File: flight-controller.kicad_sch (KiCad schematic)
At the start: 21 parts, among them U1 STM32WB55CEUx, X1 32MHz, X2 32kHz768

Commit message: added gitignore, schematic updated
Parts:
- added C16, C17: 100n, symbol Device:C
- added C18, C19: 4.7uF, symbol Device:C
- added J1: Conn_Coaxial, symbol Connector:Conn_Coaxial
- added J2: TC2030, Connector:Tag-Connect_TC2030-IDC-FP_2x03_P1.27mm_Vertical, symbol Connector:Conn_ARM_SWD_TagConnect_TC2030
- added J3: USB_C_Receptacle_USB2.0_16P, symbol Connector:USB_C_Receptacle_USB2.0_16P
- added R1, R3, R4: 5k1, symbol Device:R
- added R2: 100, symbol Device:R
- added SW1: SW_Push, symbol Switch:SW_Push
- added U2: DLF162500LT-5028A1, DLF-4_1P6X0P8, symbol TDK_LPF:DLF162500LT-5028A1
- added U3: USBLC6-2SC6, Package_TO_SOT_SMD:SOT-23-6, symbol Power_Protection:USBLC6-2SC6
- added U4: MIC5365-3.3YD5, Package_TO_SOT_SMD:SOT-23-5, symbol Regulator_Linear:MIC5365-3.3YD5
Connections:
- net +3V3: now also C19.1, J2.1 (VCC), SW1.2, U4.5 (VOUT)
- net GND: now also C16.2, C17.2, C18.2, C19.2, J1.2 (Ext), J2.5 (GND), J3.A1 (GND), J3.A12 (GND), J3.B1 (GND), J3.B12 (GND), J3.S1 (SHIELD), R1.2, R3.2, R4.2, U2.2 (GND), U2.4 (GND), U3.2 (GND), U4.2 (GND)
- net RF_MATCH: now reaches C15.1, L3.2
- net RF_MATCH: now also U2.1 (IN)
- net USB_D-: now reaches U1.37 (PA11)
- net USB_D-: now also U3.6 (I/O1)
- net USB_D+: now reaches U1.38 (PA12)
- net USB_D+: now also U3.4 (I/O2)
- net SWD_DIO: now reaches U1.39 (PA13)
- net SWD_DIO: now also J2.2 (SWDIO)
- net BOOT0: now reaches U1.4 (PH3)
- net BOOT0: now also C17.1, R1.1, R2.1
- net SWCLK: now reaches U1.41 (PA14)
- net SWCLK: now also J2.4 (SWCLK)
- net at U1.43 (PB3): now also J2.6 (SWO)
- net SWD_NRST: now reaches U1.7 (NRST)
- net SWD_NRST: now also C16.1, J2.3 (~{RESET})
- new net: R2.2, SW1.1
- new net: J3.B5 (CC2), R3.1
- new net: J3.A5 (CC1), R4.1
- new net: J3.A7 (D-), J3.B7 (D-), U3.1 (I/O1)
- new net: J3.A6 (D+), J3.B6 (D+), U3.3 (I/O2)
- new net +5V: C18.1, J3.A4 (VBUS), J3.A9 (VBUS), J3.B4 (VBUS), J3.B9 (VBUS), U3.5 (VBUS), U4.1 (VIN), U4.3 (EN)
- new net RF_NET: J1.1 (In), U2.3 (OUT)
- no-connect marks 0 -> 2
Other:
- moved on the sheet: C1, C10, C11, C12, C13, C14, C15, C2, C3, C4, C5, C6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

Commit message: added outline of imu, wip
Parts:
- added C20: 10n, symbol Device:C
- added C21, C22: 100n, symbol Device:C
- added C23: 2n2, symbol Device:C
- added R5, R6: 2k2, symbol Device:R
- added U5: MPU-6050, Sensor_Motion:InvenSense_QFN-24_4x4mm_P0.5mm, symbol Sensor_Motion:MPU-6050
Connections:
- net +3V3: now also C20.1, C21.1, R5.2, R6.2, U5.13 (VDD), U5.8 (VLOGIC)
- net GND: now also C20.2, C21.2, C22.2, C23.2, U5.1 (CLKIN), U5.11 (FSYNC), U5.18 (GND), U5.9 (AD0)
- net SCL: now reaches U1.5 (PB8)
- net SCL: now also R5.1, U5.23 (SCL)
- net SDA: now reaches U1.6 (PB9)
- net SDA: now also R6.1, U5.24 (SDA)
- new net: C22.1, U5.10 (REGOUT)
- new net: C23.1, U5.20 (CPOUT)
- no-connect marks 2 -> 4

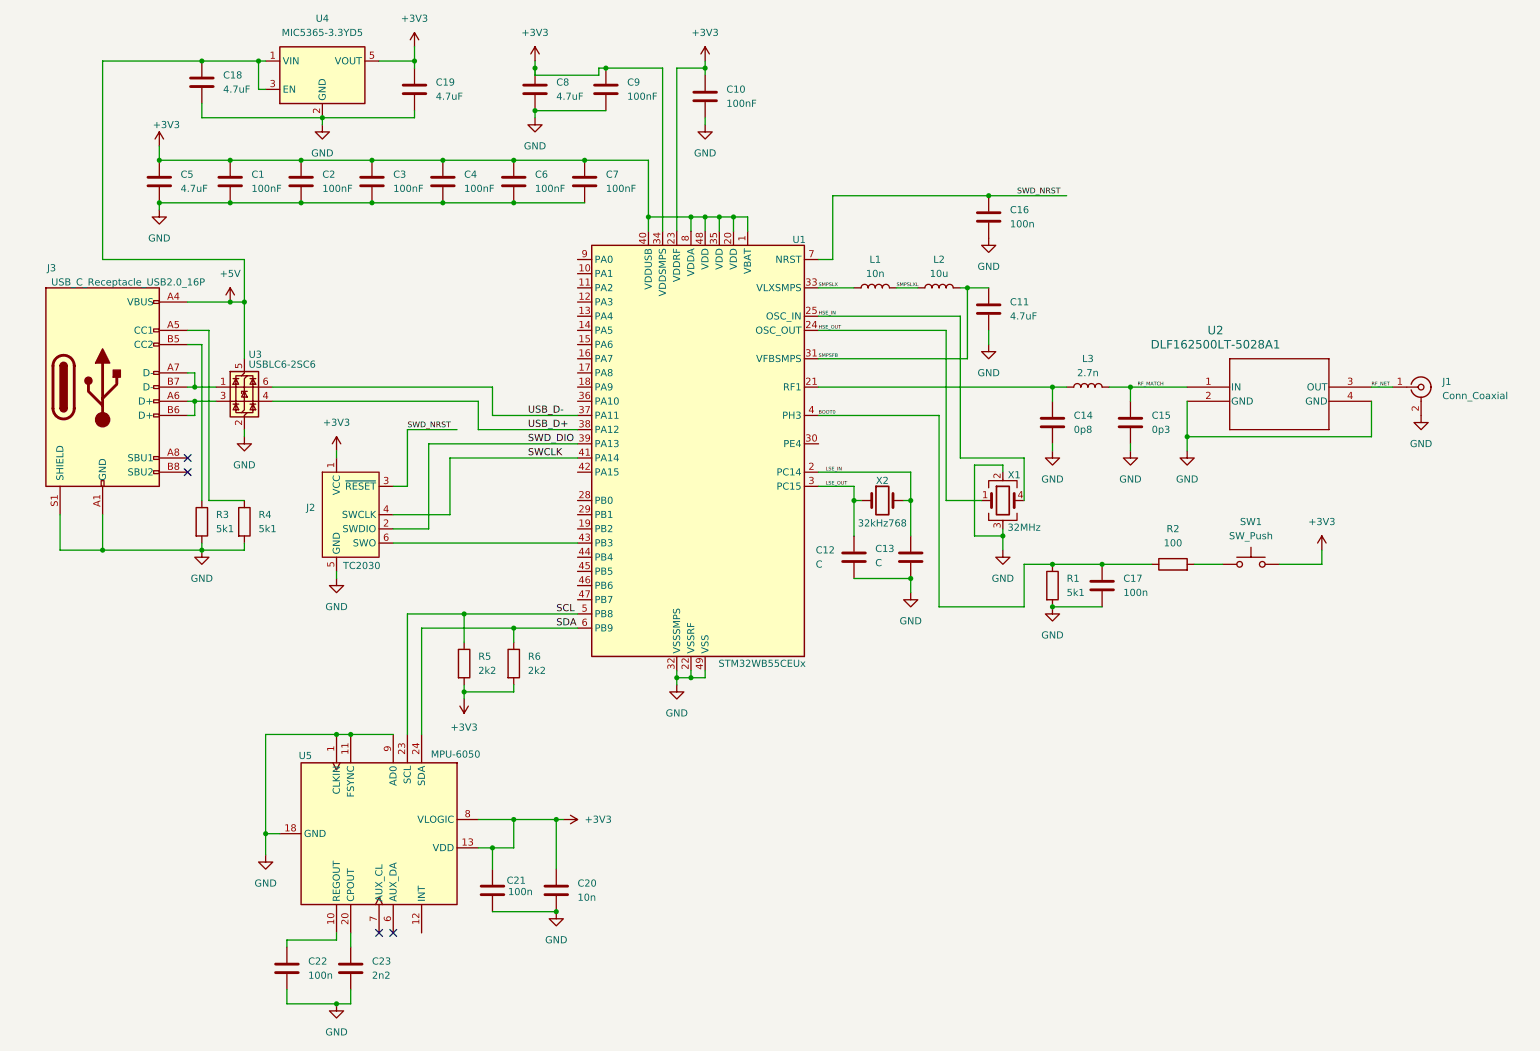
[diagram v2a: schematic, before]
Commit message: added footprints, started BOM
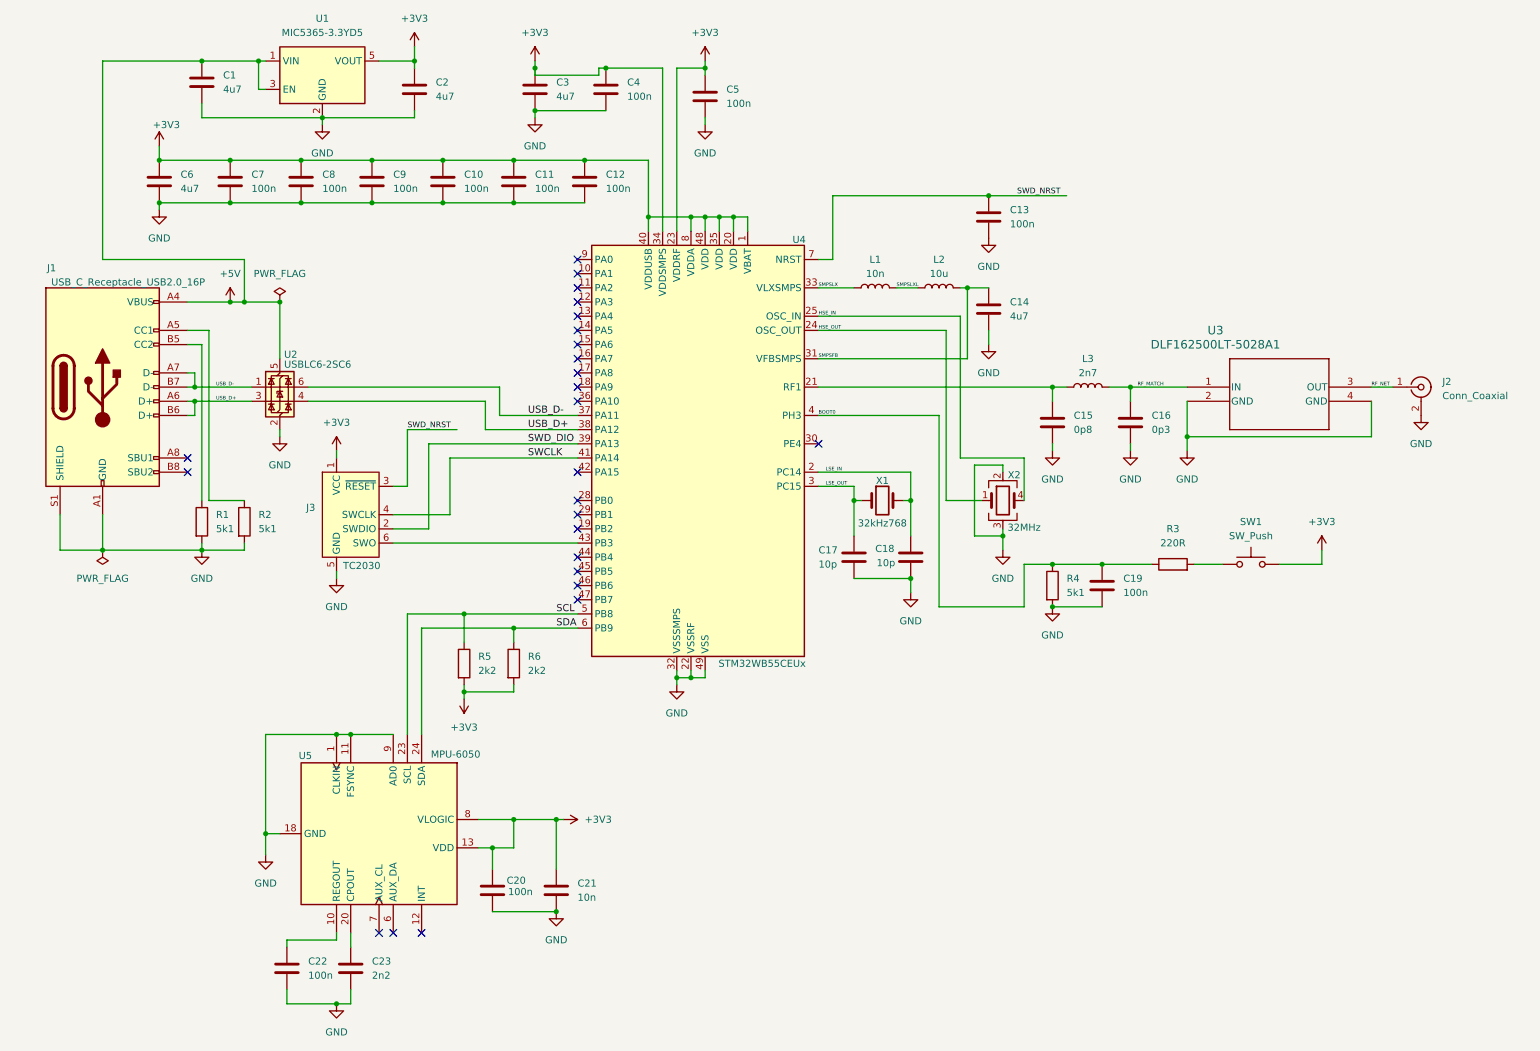
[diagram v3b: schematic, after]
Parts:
- C1: renamed from C18; value 4.7uF -> 4u7; footprint (none) -> Capacitor_SMD:C_0603_1608Metric; Distributor Link (none) -> https://www.mouser.com/ProductDetail/KYOCERA-AVX/0603ZD475M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; Manufacturer (none) -> Kyocera AVX; Manufacturer Part # (none) -> 0603ZD475MAT2A
- C10: renamed from C4; value 100nF -> 100n; footprint (none) -> Capacitor_SMD:C_0402_1005Metric; Distributor Link (none) -> https://www.mouser.com/ProductDetail/KYOCERA-AVX/0402X7R104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; Manufacturer (none) -> Kyocera AVX; Manufacturer Part # (none) -> 0402X7R104KT7AT
- C11: renamed from C6; value 100nF -> 100n; footprint (none) -> Capacitor_SMD:C_0402_1005Metric; Distributor Link (none) -> https://www.mouser.com/ProductDetail/KYOCERA-AVX/0402X7R104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; Manufacturer (none) -> Kyocera AVX; Manufacturer Part # (none) -> 0402X7R104KT7AT
- C12: renamed from C7; value 100nF -> 100n; footprint (none) -> Capacitor_SMD:C_0402_1005Metric; Distributor Link (none) -> https://www.mouser.com/ProductDetail/KYOCERA-AVX/0402X7R104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; Manufacturer (none) -> Kyocera AVX; Manufacturer Part # (none) -> 0402X7R104KT7AT
- C13: renamed from C16; footprint (none) -> Capacitor_SMD:C_0402_1005Metric; Distributor Link (none) -> https://www.mouser.com/ProductDetail/KYOCERA-AVX/0402X7R104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; Manufacturer (none) -> Kyocera AVX; Manufacturer Part # (none) -> 0402X7R104KT7AT
- C14: renamed from C11; value 4.7uF -> 4u7; footprint (none) -> Capacitor_SMD:C_0603_1608Metric; Distributor Link (none) -> https://www.mouser.com/ProductDetail/KYOCERA-AVX/0603ZD475M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; Manufacturer (none) -> Kyocera AVX; Manufacturer Part # (none) -> 0603ZD475MAT2A
- C15: renamed from C14; footprint (none) -> Capacitor_SMD:C_0402_1005Metric
- C16: renamed from C15; footprint (none) -> Capacitor_SMD:C_0402_1005Metric
- C17: renamed from C12; value C -> 10p; footprint (none) -> Capacitor_SMD:C_0402_1005Metric
- C18: renamed from C13; value C -> 10p; footprint (none) -> Capacitor_SMD:C_0402_1005Metric
- C19: renamed from C17; footprint (none) -> Capacitor_SMD:C_0402_1005Metric; Distributor Link (none) -> https://www.mouser.com/ProductDetail/KYOCERA-AVX/0402X7R104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; Manufacturer (none) -> Kyocera AVX; Manufacturer Part # (none) -> 0402X7R104KT7AT
- C2: renamed from C19; value 4.7uF -> 4u7; footprint (none) -> Capacitor_SMD:C_0603_1608Metric; Distributor Link (none) -> https://www.mouser.com/ProductDetail/KYOCERA-AVX/0603ZD475M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; Manufacturer (none) -> Kyocera AVX; Manufacturer Part # (none) -> 0603ZD475MAT2A
- C20: renamed from C21; footprint (none) -> Capacitor_SMD:C_0402_1005Metric; Distributor Link (none) -> https://www.mouser.com/ProductDetail/KYOCERA-AVX/0402X7R104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; Manufacturer (none) -> Kyocera AVX; Manufacturer Part # (none) -> 0402X7R104KT7AT
- C21: renamed from C20; footprint (none) -> Capacitor_SMD:C_0402_1005Metric
- C22: footprint (none) -> Capacitor_SMD:C_0402_1005Metric; Distributor Link (none) -> https://www.mouser.com/ProductDetail/KYOCERA-AVX/0402X7R104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; Manufacturer (none) -> Kyocera AVX; Manufacturer Part # (none) -> 0402X7R104KT7AT
- C23: footprint (none) -> Capacitor_SMD:C_0402_1005Metric
- C3: renamed from C8; value 4.7uF -> 4u7; footprint (none) -> Capacitor_SMD:C_0603_1608Metric; Distributor Link (none) -> https://www.mouser.com/ProductDetail/KYOCERA-AVX/0603ZD475M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; Manufacturer (none) -> Kyocera AVX; Manufacturer Part # (none) -> 0603ZD475MAT2A
- C4: renamed from C9; value 100nF -> 100n; footprint (none) -> Capacitor_SMD:C_0402_1005Metric; Distributor Link (none) -> https://www.mouser.com/ProductDetail/KYOCERA-AVX/0402X7R104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; Manufacturer (none) -> Kyocera AVX; Manufacturer Part # (none) -> 0402X7R104KT7AT
- C5: renamed from C10; value 100nF -> 100n; footprint (none) -> Capacitor_SMD:C_0402_1005Metric; Distributor Link (none) -> https://www.mouser.com/ProductDetail/KYOCERA-AVX/0402X7R104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; Manufacturer (none) -> Kyocera AVX; Manufacturer Part # (none) -> 0402X7R104KT7AT
- C6: renamed from C5; value 4.7uF -> 4u7; footprint (none) -> Capacitor_SMD:C_0603_1608Metric; Distributor Link (none) -> https://www.mouser.com/ProductDetail/KYOCERA-AVX/0603ZD475M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; Manufacturer (none) -> Kyocera AVX; Manufacturer Part # (none) -> 0603ZD475MAT2A
- C7: renamed from C1; value 100nF -> 100n; footprint (none) -> Capacitor_SMD:C_0402_1005Metric; Distributor Link (none) -> https://www.mouser.com/ProductDetail/KYOCERA-AVX/0402X7R104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; Manufacturer (none) -> Kyocera AVX; Manufacturer Part # (none) -> 0402X7R104KT7AT
- C8: renamed from C2; value 100nF -> 100n; footprint (none) -> Capacitor_SMD:C_0402_1005Metric; Distributor Link (none) -> https://www.mouser.com/ProductDetail/KYOCERA-AVX/0402X7R104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; Manufacturer (none) -> Kyocera AVX; Manufacturer Part # (none) -> 0402X7R104KT7AT
- C9: renamed from C3; value 100nF -> 100n; footprint (none) -> Capacitor_SMD:C_0402_1005Metric; Distributor Link (none) -> https://www.mouser.com/ProductDetail/KYOCERA-AVX/0402X7R104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; Manufacturer (none) -> Kyocera AVX; Manufacturer Part # (none) -> 0402X7R104KT7AT
- J1: renamed from J3; footprint (none) -> Connector_USB:USB_C_Receptacle_GCT_USB4105-xx-A_16P_TopMnt_Horizontal
- J2: renamed from J1; footprint (none) -> Connector_Coaxial:U.FL_Hirose_U.FL-R-SMT-1_Vertical
- L1: footprint (none) -> Inductor_SMD:L_0402_1005Metric
- L2: footprint (none) -> Inductor_SMD:L_0805_2012Metric
- L3: value 2.7n -> 2n7; footprint (none) -> Inductor_SMD:L_0402_1005Metric
- R1: renamed from R3; footprint (none) -> Resistor_SMD:R_0402_1005Metric
- R2: renamed from R4; footprint (none) -> Resistor_SMD:R_0402_1005Metric
- R3: renamed from R2; value 100 -> 220R; footprint (none) -> Resistor_SMD:R_0402_1005Metric
- R4: renamed from R1; footprint (none) -> Resistor_SMD:R_0402_1005Metric
- R5, R6: footprint (none) -> Resistor_SMD:R_0402_1005Metric
- SW1: footprint (none) -> Button_Switch_SMD:SW_SPST_CK_RS282G05A3
- U3: renamed from U2; footprint DLF-4_1P6X0P8 -> Library:DLF-4_1P6X0P8
- X1: renamed from X2; footprint (none) -> Crystal:Crystal_SMD_2012-2Pin_2.0x1.2mm
- X2: renamed from X1; footprint (none) -> Crystal:Crystal_SMD_2016-4Pin_2.0x1.6mm
- renumbered J2 to J3, U4 to U1, U3 to U2, U1 to U4
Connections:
- net USB_D+: now also J1.A6 (D+), J1.B6 (D+), U2.3 (I/O2)
- net USB_D-: now also J1.A7 (D-), J1.B7 (D-), U2.1 (I/O1)
- no-connect marks 4 -> 25
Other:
- moved on the sheet: U2

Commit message: added 3d models, start pcb layout
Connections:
- net SCL renamed I2C1_SCL
- net SDA renamed I2C1_SDA
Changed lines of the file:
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@@
-	(wire
-		(pts
-			(xy 116.84 123.19) (xy 105.41 123.19)
-		)
-		(stroke
-			(width 0)
-			(type default)
-		)
-	)
 	(wire
 		(pts
@@
 		(pts
 			(xy 92.71 39.37) (xy 105.41 39.37)
+		)
+		(stroke
+			(width 0)
+			(type default)
+		)
+	)
+	(wire
+		(pts
+			(xy 105.41 123.19) (xy 116.84 123.19)
 		)
 		(stroke
@@
 		)
 	)
-	(label "SCL"
-		(at 113.03 120.65 0)
+	(label "I2C1_SCL"
+		(at 106.68 120.65 0)
 		(fields_autoplaced yes)
 		(effects
@@
 		)
 	)
-	(label "SDA"
-		(at 113.03 123.19 0)
+	(label "I2C1_SDA"
+		(at 106.68 123.19 0)
 		(fields_autoplaced yes)
 		(effects

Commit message: finished layout
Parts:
- removed J3: TC2030, Connector:Tag-Connect_TC2030-IDC-FP_2x03_P1.27mm_Vertical, symbol Connector:Conn_ARM_SWD_TagConnect_TC2030
- added J4: TC2030, Connector:Tag-Connect_TC2030-IDC-NL_2x03_P1.27mm_Vertical, symbol Connector:Conn_ARM_SWD_TagConnect_TC2030-NL
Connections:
- net +3V3: now also J4.1 (VCC)
- net GND: now also J4.5 (GND)
- net SWCLK: now also J4.4 (SWCLK)
- net SWD_DIO: now also J4.2 (SWDIO)
- net SWD_NRST: now also J4.3 (~{RESET})
- net at U4.43 (PB3): now also J4.6 (SWO)
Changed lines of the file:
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@@
-	)
-	(symbol
-		(lib_id "Connector:Conn_ARM_SWD_TagConnect_TC2030")
-		(at 76.2 102.87 0)
-		(unit 1)
-		(exclude_from_sim no)
-		(in_bom no)
-		(on_board yes)
-		(dnp no)
-		(property "Reference" "J3"
-			(at 69.85 101.5999 0)
-			(effects
-				(font
-					(size 1.27 1.27)
-				)
-				(justify right)
-			)
-		)
-		(property "Value" "TC2030"
-			(at 81.534 112.014 0)
-			(effects
-				(font
-					(size 1.27 1.27)
-				)
-				(justify right)
-			)
-		)
-		(property "Footprint" "Connector:Tag-Connect_TC2030-IDC-FP_2x03_P1.27mm_Vertical"
-			(at 76.2 120.65 0)
-			(effects
-				(font
-					(size 1.27 1.27)
-				)
-				(hide yes)
-			)
-		)
-		(property "Datasheet" "https://www.tag-connect.com/wp-content/uploads/bsk-pdf-manager/TC2030-CTX_1.pdf"
-			(at 76.2 118.11 0)
-			(effects
-				(font
-					(size 1.27 1.27)
-				)
-				(hide yes)
-			)
-		)
-		(property "Description" "Tag-Connect ARM Cortex SWD JTAG connector, 6 pin"
-			(at 76.2 102.87 0)
-			(effects
-				(font
-					(size 1.27 1.27)
-				)
-				(hide yes)
-			)
-		)
-		(property "Distributor Link" ""
-			(at 76.2 102.87 0)
-			(effects
-				(font
-					(size 1.27 1.27)
-				)
-				(hide yes)
-			)
-		)
-		(property "Manufacturer" ""
-			(at 76.2 102.87 0)
-			(effects
-				(font
-					(size 1.27 1.27)
-				)
-				(hide yes)
-			)
-		)
-		(property "Manufacturer Part #" ""
-			(at 76.2 102.87 0)
-			(effects
-				(font
-					(size 1.27 1.27)
-				)
-				(hide yes)
-			)
-		)
-		(pin "1"
-		)
-		(pin "2"
-		)
-		(pin "3"
-		)
-		(pin "6"
-		)
-		(pin "5"
-		)
-		(pin "4"
-		)
-		(instances
-			(project "flight-controller"
-				(path "/a5f7a25c-082f-4bc5-b533-7e16fdbf1e58"
-					(reference "J3")
-					(unit 1)
-				)
-			)
-		)
 	)
 	(symbol
@@
 					(unit 1)
 				)
+			)
+		)
+	)
+	(symbol
+		(lib_id "Connector:Conn_ARM_SWD_TagConnect_TC2030-NL")
+		(at 76.2 102.87 0)
+		(unit 1)
+		(exclude_from_sim no)
+		(in_bom no)
+		(on_board yes)
+		(dnp no)
+		(property "Reference" "J4"
+			(at 69.85 101.5999 0)
+			(effects
+				(font
+					(size 1.27 1.27)
+				)
+				(justify right)
+			)
+		)
+		(property "Value" "TC2030"
+			(at 81.788 111.76 0)
+			(effects
+				(font
+					(size 1.27 1.27)
+				)
+				(justify right)
+			)
+		)
+		(property "Footprint" "Connector:Tag-Connect_TC2030-IDC-NL_2x03_P1.27mm_Vertical"
+			(at 76.2 120.65 0)
+			(effects
+				(font
+					(size 1.27 1.27)
+				)
+				(hide yes)
+			)
+		)
+		(property "Datasheet" "https://www.tag-connect.com/wp-content/uploads/bsk-pdf-manager/TC2030-CTX_1.pdf"
+			(at 76.2 118.11 0)
+			(effects
+				(font
+					(size 1.27 1.27)
+				)
+				(hide yes)
+			)
+		)
+		(property "Description" "Tag-Connect ARM Cortex SWD JTAG connector, 6 pin, no legs"
+			(at 76.2 102.87 0)
+			(effects
+				(font
+					(size 1.27 1.27)
+				)
+				(hide yes)
+			)
+		)
+		(pin "3"
+		)
+		(pin "5"
+		)
+		(pin "4"
+		)
+		(pin "1"
+		)
+		(pin "2"
+		)
+		(pin "6"
+		)
+		(instances
+			(project ""
+				(path "/a5f7a25c-082f-4bc5-b533-7e16fdbf1e58"
+					(reference "J4")
+					(unit 1)
+				)

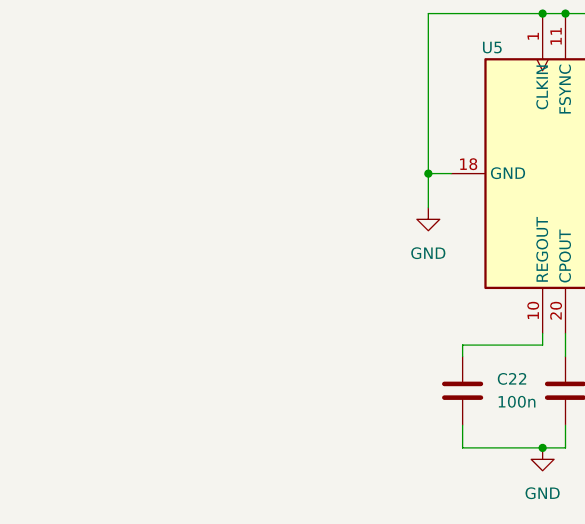
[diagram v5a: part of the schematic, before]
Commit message: begin routing, i2c layout refinement wip
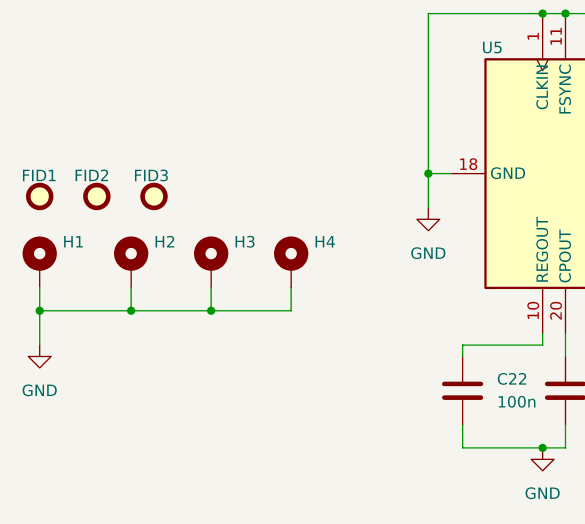
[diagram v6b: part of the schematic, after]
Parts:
- added FID1, FID2, FID3: Fiducial, Fiducial:Fiducial_1mm_Mask2mm, symbol Mechanical:Fiducial
- added H1, H2, H3, H4: MountingHole_Pad, MountingHole:MountingHole_2.2mm_M2, symbol Mechanical:MountingHole_Pad
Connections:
- net GND: now also H1.1, H2.1, H3.1, H4.1
